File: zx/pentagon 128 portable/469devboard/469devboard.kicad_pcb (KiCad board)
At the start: 2 copper layers, 10 parts, among them J1 Conn_02x17_Odd_Even, J2 Conn_ARM_JTAG_SWD_20, J3 Micro_SD_Card, U1 STM32F469IITx, Y1 NX3215SA-32.768K, Y2 NX3225GD-8.0M

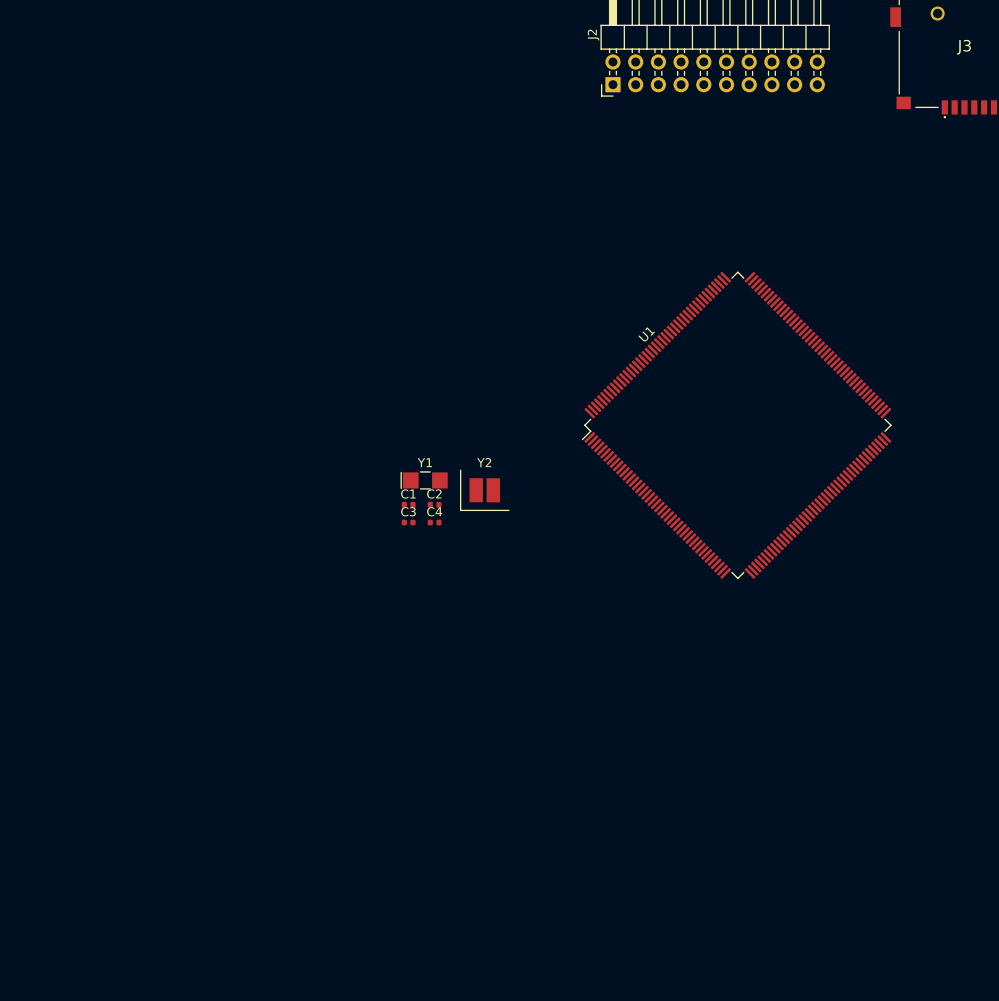
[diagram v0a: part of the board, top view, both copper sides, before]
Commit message: updated power lines
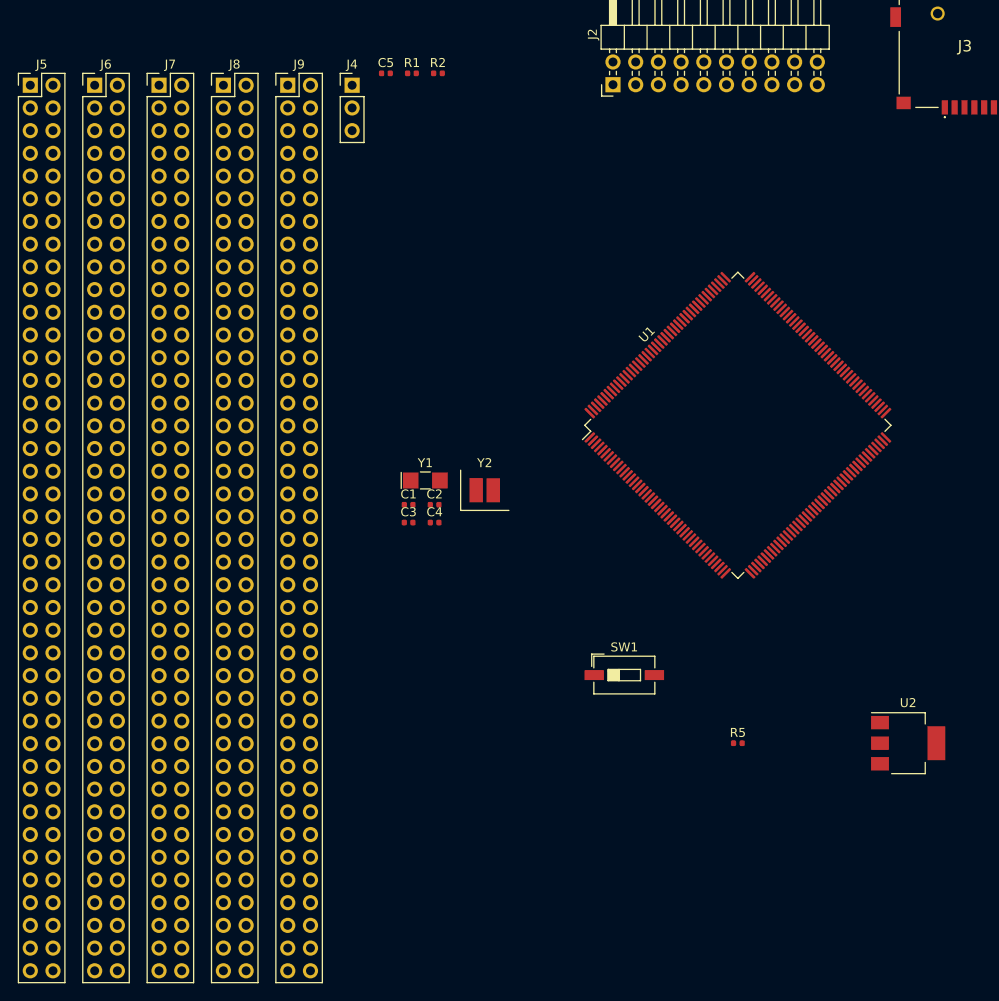
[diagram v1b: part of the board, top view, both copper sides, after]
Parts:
- added C5: 100nF, Capacitor_SMD:C_0402_1005Metric, F.Cu at (16.5, 43.2)
- added J4: Conn_01x03_Male, Connector_PinHeader_2.54mm:PinHeader_1x03_P2.54mm_Vertical, F.Cu at (12.7, 44.5)
- added J5: Conn_02x40_Counter_Clockwise, Connector_PinHeader_2.54mm:PinHeader_2x40_P2.54mm_Vertical, F.Cu at (-23.3, 44.5)
- added J6: Conn_02x40_Counter_Clockwise, Connector_PinHeader_2.54mm:PinHeader_2x40_P2.54mm_Vertical, F.Cu at (-16.1, 44.5)
- added J7: Conn_02x40_Counter_Clockwise, Connector_PinHeader_2.54mm:PinHeader_2x40_P2.54mm_Vertical, F.Cu at (-8.87, 44.5)
- added J8: Conn_02x40_Counter_Clockwise, Connector_PinHeader_2.54mm:PinHeader_2x40_P2.54mm_Vertical, F.Cu at (-1.67, 44.5)
- added J9: Conn_02x40_Counter_Clockwise, Connector_PinHeader_2.54mm:PinHeader_2x40_P2.54mm_Vertical, F.Cu at (5.53, 44.5)
- added R1: 10k, Resistor_SMD:R_0402_1005Metric, F.Cu at (19.4, 43.2)
- added R2: 100k, Resistor_SMD:R_0402_1005Metric, F.Cu at (22.3, 43.2)
- added R5: 100k, Resistor_SMD:R_0402_1005Metric, F.Cu at (55.9, 118.1)
- added SW1: SW_Push, Button_Switch_SMD:SW_DIP_SPSTx01_Slide_6.7x4.1mm_W6.73mm_P2.54mm_LowProfile_JPin, F.Cu at (43.2, 110.5)
- added U2: LD1117S33TR_SOT223, Package_TO_SOT_SMD:SOT-223-3_TabPin2, F.Cu at (74.9, 118.1)
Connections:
- J2 pad 1: (no net) -> +3V3
- J2 pad 10: Net-(J2-Pad10) -> GND
- J2 pad 12: Net-(J2-Pad10) -> GND
- J2 pad 14: Net-(J2-Pad10) -> GND
- J2 pad 16: Net-(J2-Pad10) -> GND
- J2 pad 18: Net-(J2-Pad10) -> GND
- J2 pad 2: (no net) -> +3V3
- J2 pad 20: Net-(J2-Pad10) -> GND
- J2 pad 4: Net-(J2-Pad10) -> GND
- J2 pad 6: Net-(J2-Pad10) -> GND
- J2 pad 8: Net-(J2-Pad10) -> GND
- U1 pad 100: (no net) -> /DSI_VDD12
- U1 pad 106: (no net) -> /DSI_VDD12
- U1 pad 118: (no net) -> +3V3
- U1 pad 131: (no net) -> +3V3
- U1 pad 136: (no net) -> +3V3
- U1 pad 149: (no net) -> +3V3
- U1 pad 15: (no net) -> +3V3
- U1 pad 159: (no net) -> +3V3
- U1 pad 166: GND -> Net-(R1-Pad1)
- U1 pad 172: (no net) -> +3V3
- U1 pad 23: (no net) -> +3V3
- U1 pad 36: (no net) -> +3V3
- U1 pad 49: (no net) -> +3V3
- U1 pad 6: (no net) -> Net-(J4-Pad2)
- U1 pad 62: (no net) -> +3V3
- U1 pad 72: (no net) -> +3V3
- U1 pad 82: (no net) -> +3V3
- U1 pad 96: (no net) -> +3V3
- U1 pad 99: (no net) -> +3V3

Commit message: upadted connectors
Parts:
- added BT1: cr1220 holder, Battery:BatteryHolder_LINX_BAT-HLD-012-SMT, F.Cu at (67.3, 152.4)
- added C10: 100nF, Capacitor_SMD:C_0402_1005Metric, F.Cu at (58.9, 160.7)
- added C11: 1uF, Capacitor_SMD:C_0402_1005Metric, F.Cu at (40.3, 154.0)
- added C12: 100nF, Capacitor_SMD:C_0402_1005Metric, F.Cu at (61.8, 160.7)
- added C13: 2.2uF, Capacitor_SMD:C_0402_1005Metric, F.Cu at (61.8, 162.7)
- added C14: 4.7uF, Capacitor_SMD:C_0402_1005Metric, F.Cu at (40.3, 152.0)
- added C15: 4.7uF, Capacitor_SMD:C_0402_1005Metric, F.Cu at (64.7, 170.6)
- added C16: 1uF, Capacitor_SMD:C_0402_1005Metric, F.Cu at (86.2, 157.7)
- added C17: 100nF, Capacitor_SMD:C_0402_1005Metric, F.Cu at (61.8, 164.7)
- added C18: 1uF, Capacitor_SMD:C_0402_1005Metric, F.Cu at (58.9, 167.4)
- added C19: 100nF, Capacitor_SMD:C_0402_1005Metric, F.Cu at (64.7, 160.7)
- added C20: 100nF, Capacitor_SMD:C_0402_1005Metric, F.Cu at (83.3, 159.7)
- added C21: 100nF, Capacitor_SMD:C_0402_1005Metric, F.Cu at (67.6, 160.7)
- added C22: 100nF, Capacitor_SMD:C_0402_1005Metric, F.Cu at (64.7, 162.7)
- added C23: 100nF, Capacitor_SMD:C_0402_1005Metric, F.Cu at (61.8, 166.6)
- added C24: 100nF, Capacitor_SMD:C_0402_1005Metric, F.Cu at (58.9, 169.4)
- added C25: 100nF, Capacitor_SMD:C_0402_1005Metric, F.Cu at (58.9, 173.4)
- added C26: 100nF, Capacitor_SMD:C_0402_1005Metric, F.Cu at (99.2, 146.1)
- added C27: 100nF, Capacitor_SMD:C_0402_1005Metric, F.Cu at (67.6, 162.7)
- added C28: 100nF, Capacitor_SMD:C_0402_1005Metric, F.Cu at (64.7, 166.6)
- added C29: 100nF, Capacitor_SMD:C_0402_1005Metric, F.Cu at (61.8, 168.6)
- added C30: 100nF, Capacitor_SMD:C_0402_1005Metric, F.Cu at (58.9, 171.4)
- added C31: 100nF, Capacitor_SMD:C_0402_1005Metric, F.Cu at (70.5, 160.7)
- added C32: 100nF, Capacitor_SMD:C_0402_1005Metric, F.Cu at (83.3, 161.7)
- added C33: 100nF, Capacitor_SMD:C_0402_1005Metric, F.Cu at (73.4, 160.7)
- added C34: 100nF, Capacitor_SMD:C_0402_1005Metric, F.Cu at (70.5, 162.7)
- added C35: 100nF, Capacitor_SMD:C_0402_1005Metric, F.Cu at (64.7, 164.7)
- added C36: 100nF, Capacitor_SMD:C_0402_1005Metric, F.Cu at (67.6, 168.6)
- added C37: 100nF, Capacitor_SMD:C_0402_1005Metric, F.Cu at (64.7, 168.6)
- added C6: 2.2uF, Capacitor_SMD:C_0402_1005Metric, F.Cu at (61.8, 170.6)
- added C7: 2.2uF, Capacitor_SMD:C_0402_1005Metric, F.Cu at (96.2, 146.1)
- added C8: 10uF, Capacitor_SMD:C_0402_1005Metric, F.Cu at (83.3, 157.7)
- added C9: 10uF, Capacitor_SMD:C_0402_1005Metric, F.Cu at (58.9, 163.5)
- added J10: USB_B_Mini, Connector_USB:USB_Mini-B_Lumberg_2486_01_Horizontal, F.Cu at (88.3, 149.8)
- added J11: DSI, Connector_PinHeader_2.54mm:PinHeader_1x06_P2.54mm_Vertical, F.Cu at (79.5, 147.4)
- added R3: 10k, Resistor_SMD:R_0402_1005Metric, F.Cu at (67.6, 164.7)
- added R4: 0, Resistor_SMD:R_0402_1005Metric, F.Cu at (96.2, 148.1)
- added R6: 10k, Resistor_SMD:R_0402_1005Metric, F.Cu at (70.5, 164.7)
- added R7: 10k, Resistor_SMD:R_0402_1005Metric, F.Cu at (67.6, 166.6)
- added R8: 10k, Resistor_SMD:R_0402_1005Metric, F.Cu at (58.9, 165.5)
- added R9: 10k, Resistor_SMD:R_0402_1005Metric, F.Cu at (38.1, 99.1)
- J5, J6, J7, J8: value Conn_02x40_Counter_Clockwise -> Conn_02x40_Odd_Even
- moved J9 218.7 mm to (223.5, 26.7)
- moved J6 153.3 mm to (16.5, 194.3), turned to 90 degrees
- moved J5 129.5 mm to (104.1, 21.6), turned to 270 degrees
- moved J7 116.8 mm to (108.0, 44.5)
- moved J1 62.0 mm to (143.5, 105.4), turned to 180 degrees
- moved C1 15.7 mm to (22.9, 106.7)
- moved C2 15.7 mm to (25.8, 106.7)
- moved Y2 15.7 mm to (31.4, 105.1)
- moved C3 15.7 mm to (22.9, 108.7)
- moved C4 15.7 mm to (25.8, 108.7)
- moved Y1 15.7 mm to (24.7, 104.0)
- moved J8 7.86 mm to (0.00, 36.8)
- turned U1 to 0 degrees
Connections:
- net /FMC_D2 renamed PD0
- net /FMC_D3 renamed PD1
- net /FMC_NE1 renamed PD7
- net /FMC_NOE renamed PD4
- net /FMC_NWE renamed PD5
- net /SDIO_CK renamed PC12
- net /SDIO_D0 renamed PC8
- net /SDIO_D1 renamed PC9
- net /SDIO_D2 renamed PC10
- net /SDIO_D3 renamed PC11
- net /SYS_JTCK_SWCLK renamed PA14
- net /SYS_JTMS_SWDIO renamed PA13
- J1 pad 13: /FMC_D15 -> PD10
- J1 pad 15: /FMC_D13 -> PD8
- J1 pad 16: /FMC_D14 -> PD9
- J1 pad 17: /FMC_D11 -> PE14
- J1 pad 18: /FMC_D12 -> PE15
- J1 pad 19: /FMC_D9 -> PE12
- J1 pad 2: /T_CLK -> PA5
- J1 pad 20: /FMC_D10 -> PE13
- J1 pad 21: /FMC_D7 -> PE10
- J1 pad 22: /FMC_D8 -> PE11
- J1 pad 23: /FMC_D5 -> PE8
- J1 pad 24: /FMC_D6 -> PE9
- J1 pad 26: /FMC_D4 -> PE7
- J1 pad 27: /FMC_D1 -> PD15
- J1 pad 3: /PEN -> PD12
- J1 pad 30: /FMC_D0 -> PD14
- J1 pad 34: /FMC_A16 -> PD11
- J1 pad 5: /T_MISO -> PA6
- J1 pad 6: /T_MOSI -> PA7
- J2 pad 11: (no net) -> Net-(J2-Pad11)
- J2 pad 17: (no net) -> Net-(J2-Pad17)
- J2 pad 19: (no net) -> Net-(J2-Pad19)
- J4 pad 3: (no net) -> Net-(BT1-Pad1)
- J5 pad 2: (no net) -> PI1
- J5 pad 4: (no net) -> PI3
- J6 pad 1: (no net) -> PC4
- J6 pad 10: (no net) -> PA5
- J6 pad 11: (no net) -> PG0
- J6 pad 12: (no net) -> PA6
- J6 pad 13: (no net) -> PG1
- J6 pad 14: (no net) -> PA7
- J6 pad 15: (no net) -> PE7
- J6 pad 16: (no net) -> PF11
- J6 pad 17: (no net) -> PE8
- J6 pad 18: (no net) -> PF12
- J6 pad 19: (no net) -> PE9
- J6 pad 2: (no net) -> PH4
- J6 pad 20: (no net) -> PF13
- J6 pad 21: (no net) -> PE10
- J6 pad 22: (no net) -> PF14
- J6 pad 23: (no net) -> PE11
- J6 pad 24: (no net) -> PF15
- J6 pad 25: (no net) -> PE12
- J6 pad 26: (no net) -> PB10
- J6 pad 27: (no net) -> PE13
- J6 pad 28: (no net) -> PB11
- J6 pad 29: (no net) -> PE14
- J6 pad 3: (no net) -> PC5
- J6 pad 30: (no net) -> PH6
- J6 pad 31: (no net) -> PE15
- J6 pad 32: (no net) -> PH7
- J6 pad 34: (no net) -> PB12
- J6 pad 36: (no net) -> PB13
- J6 pad 38: (no net) -> PB14
- J6 pad 4: (no net) -> PH5
- J6 pad 40: (no net) -> PB15
- J6 pad 5: (no net) -> PB0
- J6 pad 6: (no net) -> PA3
- J6 pad 7: (no net) -> PB1
- J6 pad 8: (no net) -> PA4
- J6 pad 9: (no net) -> PB2
- J7 pad 35: (no net) -> PI0
- J7 pad 37: (no net) -> PA12
- J7 pad 39: (no net) -> PA11
- J7 pad 41: (no net) -> PA10
- J7 pad 43: (no net) -> PA9
- J7 pad 45: (no net) -> PA8
- J7 pad 47: (no net) -> PC7
- J7 pad 49: (no net) -> PC6
- J7 pad 51: (no net) -> PG8
- J7 pad 53: (no net) -> PG7
- J7 pad 55: (no net) -> PG6
- J7 pad 57: (no net) -> PG5
- J7 pad 59: (no net) -> PG4
- J7 pad 61: (no net) -> PG3
- J7 pad 63: (no net) -> PG2
- J7 pad 65: (no net) -> PD15
- J7 pad 67: (no net) -> PD14
- J7 pad 69: (no net) -> PD13
- J7 pad 71: (no net) -> PD12
- J7 pad 73: (no net) -> PD11
- J7 pad 75: (no net) -> PD10
- J7 pad 77: (no net) -> PD9
- J7 pad 79: (no net) -> PD8
- J8 pad 37: (no net) -> PE2
- J8 pad 39: (no net) -> PE3
- J8 pad 41: (no net) -> PE4
- J8 pad 43: (no net) -> PE5
- J8 pad 45: (no net) -> PE6
- J8 pad 47: (no net) -> PF0
- J8 pad 48: (no net) -> PI8
- J8 pad 49: (no net) -> PF1
- J8 pad 50: (no net) -> PC13
- J8 pad 51: (no net) -> PF2
- J8 pad 52: (no net) -> PI9
- J8 pad 53: (no net) -> PF3
- J8 pad 54: (no net) -> PI10
- J8 pad 55: (no net) -> PF4
- J8 pad 56: (no net) -> PI11
- J8 pad 57: (no net) -> PF5
- J8 pad 58: (no net) -> PC0
- J8 pad 59: (no net) -> PF6
- J8 pad 60: (no net) -> PC1
- J8 pad 61: (no net) -> PF7
- J8 pad 62: (no net) -> PC2
- J8 pad 63: (no net) -> PF8
- J8 pad 64: (no net) -> PC3
- J8 pad 65: (no net) -> PF9
- J8 pad 66: (no net) -> PA0
- J8 pad 67: (no net) -> PF10
- J8 pad 68: (no net) -> PA1
- J8 pad 70: (no net) -> PA2
- J8 pad 72: (no net) -> PH2
- J8 pad 74: (no net) -> PH3
- R5 pad 1: (no net) -> Net-(J10-Pad4)
- U1 pad 1: (no net) -> PE2
- U1 pad 101: (no net) -> Net-(J11-Pad1)
- U1 pad 102: (no net) -> Net-(J11-Pad2)
- U1 pad 104: (no net) -> Net-(J11-Pad3)
- U1 pad 105: (no net) -> Net-(J11-Pad4)
- U1 pad 107: (no net) -> Net-(J11-Pad5)
- U1 pad 108: (no net) -> Net-(J11-Pad6)
- U1 pad 11: (no net) -> PI9
- U1 pad 110: (no net) -> PG2
- U1 pad 111: (no net) -> PG3
- U1 pad 112: (no net) -> PG4
- U1 pad 113: (no net) -> PG5
- U1 pad 114: (no net) -> PG6
- U1 pad 115: (no net) -> PG7
- U1 pad 116: (no net) -> PG8
- U1 pad 119: (no net) -> PC6
- U1 pad 12: (no net) -> PI10
- U1 pad 120: (no net) -> PC7
- U1 pad 123: (no net) -> PA8
- U1 pad 124: (no net) -> PA9
- U1 pad 125: (no net) -> PA10
- U1 pad 126: (no net) -> PA11
- U1 pad 127: (no net) -> PA12
- U1 pad 129: (no net) -> Net-(C7-Pad1)
- U1 pad 13: (no net) -> PI11
- U1 pad 132: (no net) -> PI0
- U1 pad 133: (no net) -> PI1
- U1 pad 134: (no net) -> PI3
- U1 pad 16: (no net) -> PF0
- U1 pad 17: (no net) -> PF1
- U1 pad 171: (no net) -> Net-(R9-Pad1)
- U1 pad 18: (no net) -> PF2
- U1 pad 19: (no net) -> PF3
- U1 pad 2: (no net) -> PE3
- U1 pad 20: (no net) -> PF4
- U1 pad 21: (no net) -> PF5
- U1 pad 24: (no net) -> PF6
- U1 pad 25: (no net) -> PF7
- U1 pad 26: (no net) -> PF8
- U1 pad 27: (no net) -> PF9
- U1 pad 28: (no net) -> PF10
- U1 pad 3: (no net) -> PE4
- U1 pad 32: (no net) -> PC0
- U1 pad 33: (no net) -> PC1
- U1 pad 34: (no net) -> PC2
- U1 pad 35: (no net) -> PC3
- U1 pad 38: (no net) -> /VDD_REF+
- U1 pad 39: (no net) -> /VDD_A
- U1 pad 4: (no net) -> PE5
- U1 pad 40: (no net) -> PA0
- U1 pad 41: (no net) -> PA1
- U1 pad 42: (no net) -> PA2
- U1 pad 43: (no net) -> PH2
- U1 pad 44: (no net) -> PH3
- U1 pad 45: (no net) -> PH4
- U1 pad 46: (no net) -> PH5
- U1 pad 47: (no net) -> PA3
- U1 pad 48: (no net) -> Net-(R3-Pad1)
- U1 pad 5: (no net) -> PE6
- U1 pad 50: (no net) -> PA4
- U1 pad 51: /T_CLK -> PA5
- U1 pad 52: /T_MISO -> PA6
- U1 pad 53: /T_MOSI -> PA7
- U1 pad 54: (no net) -> PC4
- U1 pad 55: (no net) -> PC5
- U1 pad 56: (no net) -> PB0
- U1 pad 57: (no net) -> PB1
- U1 pad 58: (no net) -> PB2
- U1 pad 59: (no net) -> PF11
- U1 pad 60: (no net) -> PF12
- U1 pad 63: (no net) -> PF13
- U1 pad 64: (no net) -> PF14
- U1 pad 65: (no net) -> PF15
- U1 pad 66: (no net) -> PG0
- U1 pad 67: (no net) -> PG1
- U1 pad 68: /FMC_D4 -> PE7
- U1 pad 69: /FMC_D5 -> PE8
- U1 pad 7: (no net) -> PI8
- U1 pad 70: /FMC_D6 -> PE9
- U1 pad 73: /FMC_D7 -> PE10
- U1 pad 74: /FMC_D8 -> PE11
- U1 pad 75: /FMC_D9 -> PE12
- U1 pad 76: /FMC_D10 -> PE13
- U1 pad 77: /FMC_D11 -> PE14
- U1 pad 78: /FMC_D12 -> PE15
- U1 pad 79: (no net) -> PB10
- U1 pad 8: (no net) -> PC13
- U1 pad 80: (no net) -> PB11
- U1 pad 81: (no net) -> Net-(C6-Pad1)
- U1 pad 83: (no net) -> PH6
- U1 pad 84: (no net) -> PH7
- U1 pad 85: (no net) -> PB12
- U1 pad 86: (no net) -> PB13
- U1 pad 87: (no net) -> PB14
- U1 pad 88: (no net) -> PB15
- U1 pad 89: /FMC_D13 -> PD8
- U1 pad 90: /FMC_D14 -> PD9
- U1 pad 91: /FMC_D15 -> PD10
- U1 pad 92: /FMC_A16 -> PD11
- U1 pad 93: /PEN -> PD12
- U1 pad 94: (no net) -> PD13
- U1 pad 97: /FMC_D0 -> PD14
- U1 pad 98: /FMC_D1 -> PD15
- U2 pad 3: (no net) -> +5V

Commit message: update devboard routing
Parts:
- removed BT1: cr1220 holder, Battery:BatteryHolder_LINX_BAT-HLD-012-SMT
- removed J10: USB_B_Mini, Connector_USB:USB_Mini-B_Lumberg_2486_01_Horizontal
- removed R4: 0, Resistor_SMD:R_0402_1005Metric
- added C38: 100nF, Capacitor_SMD:C_0402_1005Metric, B.Cu at (118.2, 74.7)
- added C39: 100nF, Capacitor_SMD:C_0402_1005Metric, B.Cu at (119.4, 74.7)
- added C40: 100nF, Capacitor_SMD:C_0402_1005Metric, B.Cu at (111.6, 75.2)
- added C41: 100nF, Capacitor_SMD:C_0402_1005Metric, B.Cu at (112.8, 75.2)
- added C42: 100nF, Capacitor_SMD:C_0402_1005Metric, B.Cu at (111.2, 81.5)
- added C43: 100nF, Capacitor_SMD:C_0402_1005Metric, B.Cu at (111.2, 80.4)
- added C44: 100nF, Capacitor_SMD:C_0402_1005Metric, B.Cu at (111.2, 84.3)
- added C45: 100nF, Capacitor_SMD:C_0402_1005Metric, B.Cu at (111.2, 85.4)
- added C46: 100nF, Capacitor_SMD:C_0402_1005Metric, B.Cu at (124.3, 94.4)
- added C47: 100nF, Capacitor_SMD:C_0402_1005Metric, B.Cu at (123.1, 94.4)
- added C48: 100nF, Capacitor_SMD:C_0402_1005Metric, B.Cu at (111.5, 87.9)
- added C49: 100nF, Capacitor_SMD:C_0402_1005Metric, B.Cu at (111.5, 88.9)
- added FB1: GZ2012D601TF, Capacitor_SMD:C_0805_2012Metric, B.Cu at (114.3, 89.6)
- added IC1: 1072, SamacSys_Parts:1072, F.Cu at (95.1, 65.2)
- added R10: 220, Resistor_SMD:R_0402_1005Metric, F.Cu at (105.7, 88.6)
- C11, C12, C13, C14, C15, C16, C17, C18, C19, C20, C21, C22, C23, C24, C25, C26, C27, C28, C29, C30, C31, C32, C33, C34, C35, C36, C37, R1, R3, R9: moved to B.Cu
- C6, C7: footprint Capacitor_SMD:C_0402_1005Metric -> Capacitor_SMD:C_1210_3225Metric_Pad1.42x2.65mm_HandSolder
- J2: footprint Connector_PinHeader_2.54mm:PinHeader_2x10_P2.54mm_Horizontal -> Connector_PinHeader_2.54mm:PinHeader_2x10_P2.54mm_Vertical
- J3: value Micro_SD_Card -> 10033526-N3212LF; footprint pentagon128:112JTDARR -> SamacSys_Parts:10033526N3212LF
- J5: value Conn_02x40_Odd_Even -> Conn_01x35_Male; footprint Connector_PinHeader_2.54mm:PinHeader_2x40_P2.54mm_Vertical -> Connector_PinHeader_2.54mm:PinHeader_1x35_P2.54mm_Vertical
- J6: value Conn_02x40_Odd_Even -> Conn_01x36_Male; footprint Connector_PinHeader_2.54mm:PinHeader_2x40_P2.54mm_Vertical -> Connector_PinHeader_2.54mm:PinHeader_1x36_P2.54mm_Vertical
- J7: value Conn_02x40_Odd_Even -> Conn_01x23_Male; footprint Connector_PinHeader_2.54mm:PinHeader_2x40_P2.54mm_Vertical -> Connector_PinHeader_2.54mm:PinHeader_1x23_P2.54mm_Vertical
- J8: value Conn_02x40_Odd_Even -> Conn_01x30_Male; footprint Connector_PinHeader_2.54mm:PinHeader_2x40_P2.54mm_Vertical -> Connector_PinHeader_2.54mm:PinHeader_1x30_P2.54mm_Vertical
- J9: value Conn_02x40_Counter_Clockwise -> 104031-0811; footprint Connector_PinHeader_2.54mm:PinHeader_2x40_P2.54mm_Vertical -> SamacSys_Parts:1040310811; moved to B.Cu
- Y1: value NX3215SA-32.768K -> Q13FC1350000400; footprint Crystal:Crystal_SMD_G8-2Pin_3.2x1.5mm_HandSoldering -> Crystal:Crystal_SMD_G8-2Pin_3.2x1.5mm
- Y2: value NX3225GD-8.0M -> ABM3B-8.000MHZ-10-1-U-T; footprint pentagon128:Crystal_SMD_3225-4Pin_3.2x2.5mm_HandSoldering -> Crystal:Crystal_SMD_Abracon_ABM3B-4Pin_5.0x3.2mm
- moved C5 136.1 mm to (151.1, 63.1)
- moved R8 130.9 mm to (144.0, 66.0), turned to 180 degrees
- moved R2 130.5 mm to (151.1, 64.2), turned to 180 degrees
- moved J3 125.2 mm to (164.4, 140.6), turned to 0 degrees
- moved R6 120.1 mm to (139.1, 66.0)
- moved J2 119.4 mm to (158.9, 68.8), turned to 270 degrees
- moved SW1 118.8 mm to (150.6, 59.9)
- moved R7 117.1 mm to (133.5, 69.8), turned to 270 degrees
- moved C10 116.6 mm to (166.6, 116.1), turned to 90 degrees
- moved C9 116.5 mm to (165.3, 116.1), turned to 90 degrees
- moved C30 115.8 mm to (130.8, 80.6), turned to 180 degrees
- moved R5 112.4 mm to (168.2, 123.5)
- moved C11 111.6 mm to (130.5, 88.4), turned to 180 degrees
- moved C37 111.2 mm to (124.3, 74.7), turned to 270 degrees
- moved C35 110.5 mm to (128.9, 74.7), turned to 270 degrees
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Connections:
- C18 pad 1: /VDD_REF+ -> /VDD_A
- C19 pad 1: /VDD_REF+ -> /VDD_A
- C4 pad 1: /HSE_OUT -> Net-(C4-Pad1)
- J3 pad 1: PC10 -> +5V
- J3 pad 2: PC11 -> (no net)
- J3 pad 4: (no net) -> Net-(J3-Pad4)
- J3 pad 5: PC12 -> GND
- J5 pad 1: (no net) -> PI1
- J5 pad 10: (no net) -> PD2
- J5 pad 11: (no net) -> PD3
- J5 pad 12: (no net) -> PD4
- J5 pad 13: (no net) -> PD5
- J5 pad 14: (no net) -> PD6
- J5 pad 15: (no net) -> PD7
- J5 pad 16: (no net) -> PG9
- J5 pad 17: (no net) -> PG10
- J5 pad 18: (no net) -> PG11
- J5 pad 19: (no net) -> PG12
- J5 pad 2: PI1 -> PI3
- J5 pad 20: (no net) -> PG13
- J5 pad 21: (no net) -> PG14
- J5 pad 22: (no net) -> PG15
- J5 pad 23: (no net) -> PB3
- J5 pad 24: (no net) -> PB4
- J5 pad 25: (no net) -> PB5
- J5 pad 26: (no net) -> PB6
- J5 pad 27: (no net) -> PB7
- J5 pad 28: (no net) -> PB8
- J5 pad 29: (no net) -> PB9
- J5 pad 3: (no net) -> PA14
- J5 pad 30: (no net) -> PE0
- J5 pad 31: (no net) -> PE1
- J5 pad 32: (no net) -> PI4
- J5 pad 33: (no net) -> PI5
- J5 pad 34: (no net) -> PI6
- J5 pad 35: (no net) -> PI7
- J5 pad 4: PI3 -> PA15
- J5 pad 5: (no net) -> PC10
- J5 pad 6: (no net) -> PC11
- J5 pad 7: (no net) -> PC12
- J5 pad 8: (no net) -> PD0
- J5 pad 9: (no net) -> PD1
- J6 pad 1: PC4 -> PH4
- J6 pad 10: PA5 -> PB0
- J6 pad 11: PG0 -> PB1
- J6 pad 12: PA6 -> PB2
- J6 pad 13: PG1 -> PF11
- J6 pad 14: PA7 -> PF12
- J6 pad 15: PE7 -> PF13
- J6 pad 16: PF11 -> PF14
- J6 pad 17: PE8 -> PF15
- J6 pad 18: PF12 -> PG0
- J6 pad 19: PE9 -> PG1
- J6 pad 2: PH4 -> PH5
- J6 pad 20: PF13 -> PE7
- J6 pad 21: PE10 -> PE8
- J6 pad 22: PF14 -> PE9
- J6 pad 23: PE11 -> PE10
- J6 pad 24: PF15 -> PE11
- J6 pad 26: PB10 -> PE13
- J6 pad 27: PE13 -> PE14
- J6 pad 28: PB11 -> PE15
- J6 pad 29: PE14 -> PB10
- J6 pad 3: PC5 -> PA3
- J6 pad 30: PH6 -> PB11
- J6 pad 31: PE15 -> PH6
- J6 pad 33: (no net) -> PB12
- J6 pad 34: PB12 -> PB13
- J6 pad 35: (no net) -> PB14
- J6 pad 36: PB13 -> PB15
- J6 pad 4: PH5 -> PA4
- J6 pad 5: PB0 -> PA5
- J6 pad 6: PA3 -> PA6
- J6 pad 7: PB1 -> PA7
- J6 pad 8: PA4 -> PC4
- J6 pad 9: PB2 -> PC5
- J7 pad 1: (no net) -> PD8
- J7 pad 10: (no net) -> PG3
- J7 pad 11: (no net) -> PG4
- J7 pad 12: (no net) -> PG5
- J7 pad 13: (no net) -> PG6
- J7 pad 14: (no net) -> PG7
- J7 pad 15: (no net) -> PG8
- J7 pad 16: (no net) -> PC6
- J7 pad 17: (no net) -> PC7
- J7 pad 18: (no net) -> PA8
- J7 pad 19: (no net) -> PA9
- J7 pad 2: (no net) -> PD9
- J7 pad 20: (no net) -> PA10
- J7 pad 21: (no net) -> PA11
- J7 pad 22: (no net) -> PA12
- J7 pad 23: (no net) -> PI0
- J7 pad 3: (no net) -> PD10
- J7 pad 4: (no net) -> PD11
- J7 pad 5: (no net) -> PD12
- J7 pad 6: (no net) -> PD13
- J7 pad 7: (no net) -> PD14
- J7 pad 8: (no net) -> PD15
- J7 pad 9: (no net) -> PG2
- J8 pad 1: (no net) -> PE2
- J8 pad 10: (no net) -> PI11
- J8 pad 11: (no net) -> PF0
- J8 pad 12: (no net) -> PF1
- J8 pad 13: (no net) -> PF2
- J8 pad 14: (no net) -> PF3
- J8 pad 15: (no net) -> PF4
- J8 pad 16: (no net) -> PF5
- J8 pad 17: (no net) -> PF6
- J8 pad 18: (no net) -> PF7
- J8 pad 19: (no net) -> PF8
- J8 pad 2: (no net) -> PE3
- J8 pad 20: (no net) -> PF9
- J8 pad 21: (no net) -> PF10
- J8 pad 22: (no net) -> PC0
- J8 pad 23: (no net) -> PC1
- J8 pad 24: (no net) -> PC2
- J8 pad 25: (no net) -> PC3
- J8 pad 26: (no net) -> PA0
- J8 pad 27: (no net) -> PA1
- J8 pad 28: (no net) -> PA2
- J8 pad 29: (no net) -> PH2
- J8 pad 3: (no net) -> PE4
- J8 pad 30: (no net) -> PH3
- J8 pad 4: (no net) -> PE5
- J8 pad 5: (no net) -> PE6
- J8 pad 6: (no net) -> PI8
- J8 pad 7: (no net) -> PC13
- J8 pad 8: (no net) -> PI9
- J8 pad 9: (no net) -> PI10
- J9 pad 1: (no net) -> PC10
- J9 pad 2: (no net) -> PC11
- J9 pad 5: (no net) -> PC12
- J9 pad 6: (no net) -> GND
- J9 pad 7: (no net) -> PC8
- J9 pad 8: (no net) -> PC9
- R5 pad 1: Net-(J10-Pad4) -> Net-(J3-Pad4)
- U1 pad 138: (no net) -> PA15
- U1 pad 144: (no net) -> PD2
- U1 pad 145: (no net) -> PD3
- U1 pad 150: (no net) -> PD6
- U1 pad 152: (no net) -> PG9
- U1 pad 153: (no net) -> PG10
- U1 pad 154: (no net) -> PG11
- U1 pad 155: (no net) -> PG12
- U1 pad 156: (no net) -> PG13
- U1 pad 157: (no net) -> PG14
- U1 pad 160: (no net) -> PG15
- U1 pad 161: (no net) -> PB3
- U1 pad 162: (no net) -> PB4
- U1 pad 163: (no net) -> PB5
- U1 pad 164: (no net) -> PB6
- U1 pad 165: (no net) -> PB7
- U1 pad 167: (no net) -> PB8
- U1 pad 168: (no net) -> PB9
- U1 pad 169: (no net) -> PE0
- U1 pad 170: (no net) -> PE1
- U1 pad 173: (no net) -> PI4
- U1 pad 174: (no net) -> PI5
- U1 pad 175: (no net) -> PI6
- U1 pad 176: (no net) -> PI7
- U1 pad 38: /VDD_REF+ -> /VDD_A
- Y2 pad 2: /HSE_OUT -> GND
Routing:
- net PA5: track 0.00 -> 111.7 mm
- net PA6: track 0.00 -> 101.8 mm
- net GND: track 0.00 -> 95.3 mm, vias 0 -> 60
- net PA14: track 0.00 -> 69.7 mm
- net +3V3: track 0.00 -> 67.9 mm, vias 0 -> 17
- net /NRST: track 0.00 -> 64.1 mm, vias 0 -> 2
- net PD12: track 0.00 -> 58.7 mm, vias 0 -> 1
- net PB15: track 0.00 -> 57.9 mm
- net PB14: track 0.00 -> 55.9 mm
- net PB13: track 0.00 -> 54.1 mm
- net PE8: track 0.00 -> 52.9 mm
- net PB12: track 0.00 -> 51.9 mm
- net PH3: track 0.00 -> 51.7 mm
- net PH7: track 0.00 -> 49.9 mm
- net PE7: track 0.00 -> 49.7 mm
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- added copper zone on In2.Cu, net +3V3
- added copper zone on B.Cu, net GND
- added copper zone on F.Cu, net GND
- added copper zone on In1.Cu, net GND
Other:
- copper layers 2 -> 4
- net class Default: clearance 0.2 -> 0.127; trace_width 0.25 -> 0.127; via_drill 0.4 -> 0.45
- net class mcu added: clearance 0.127, trace_width 0.127, via_dia 0.8, via_drill 0.45
- rule trace_clearance: 0.2 -> 0.127
- rule trace_min: 0.2 -> 0.127
- rule via_min_size: 0.4 -> 0.45
